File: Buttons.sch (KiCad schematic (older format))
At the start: 24 parts

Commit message: Probably pre-alpha version is done
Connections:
- net Button_+ renamed Button_Plus
- net Button_- renamed Button_Minus
- net Button_clock renamed Button_Clock
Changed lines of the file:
@@
 $Descr A4 11693 8268
 encoding utf-8
-Sheet 10 9
+Sheet 9 9
 Title ""
 Date ""
@@
 "Func"
 Text HLabel 3670 2030 0    50   Output ~ 0
-Button_+
+Button_Plus
 Text HLabel 3670 2470 0    50   Output ~ 0
-Button_-
+Button_Minus
 Text HLabel 3670 2910 0    50   Output ~ 0
 Button_Emh
 Text HLabel 3670 3350 0    50   Output ~ 0
-Button_clock
+Button_Clock
 Text HLabel 3670 3790 0    50   Output ~ 0
 Button_pH

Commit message: v0.1
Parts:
- gave numbers to parts that had none: 24

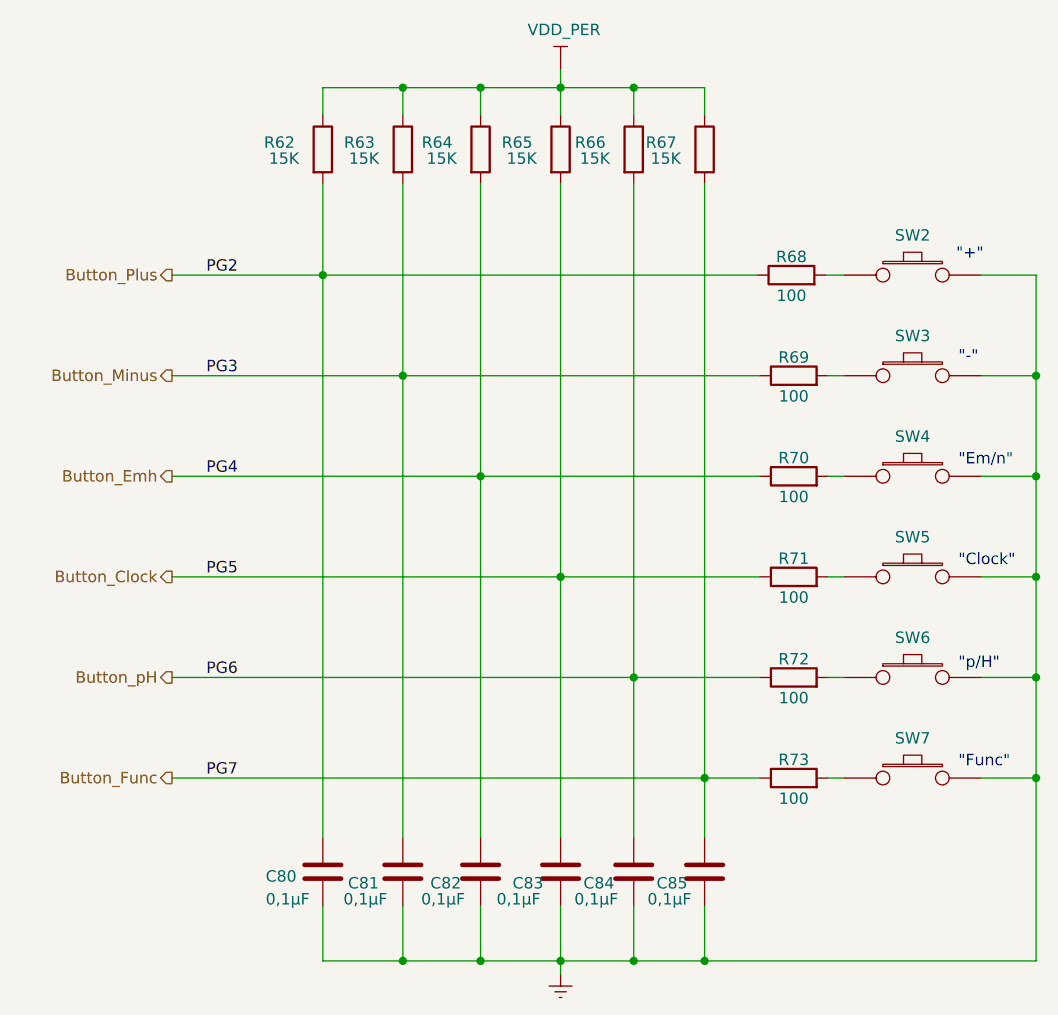
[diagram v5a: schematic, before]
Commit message: v0.3 changed sd_card holder
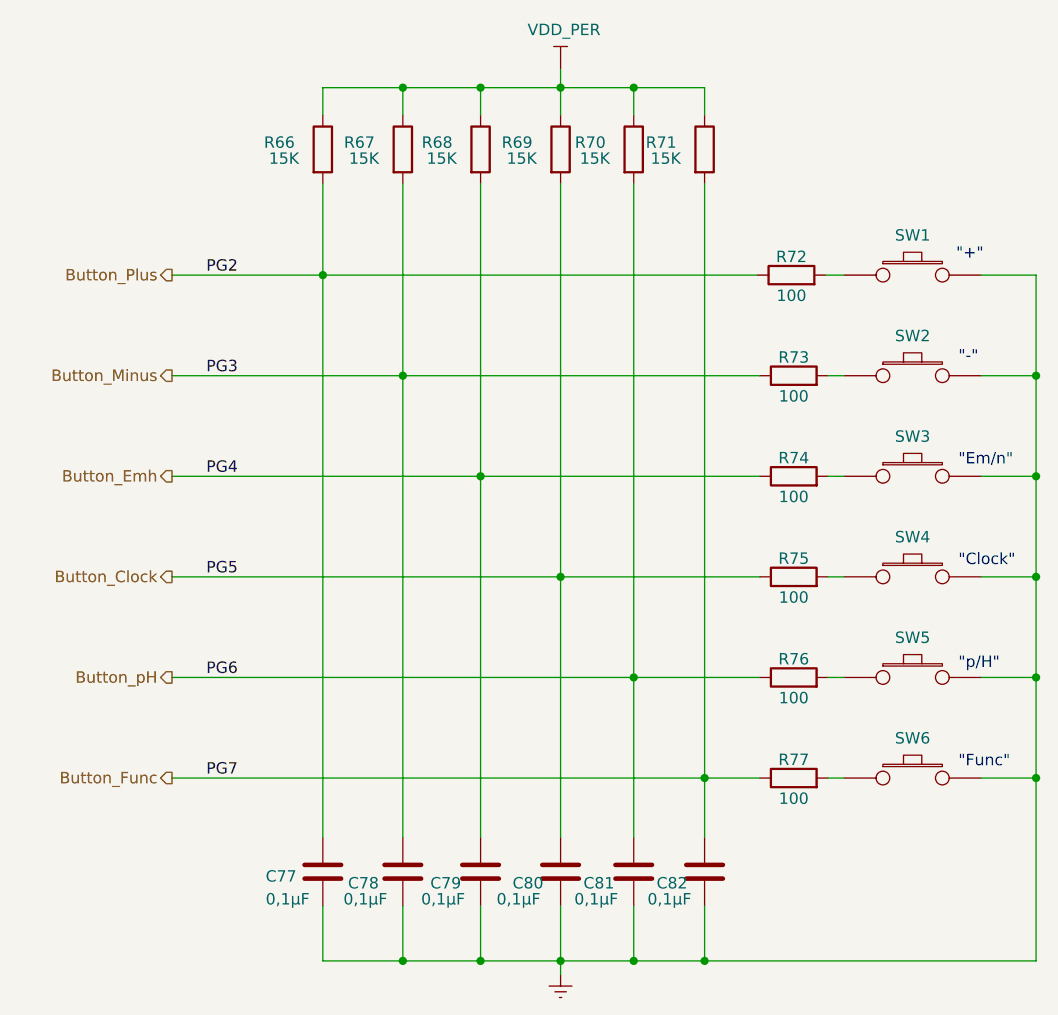
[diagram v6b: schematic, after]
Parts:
- renumbered C80 to C77, C81 to C78, C82 to C79, C83 to C80, C84 to C81, C85 to C82, R62 to R66, R63 to R67, R64 to R68, R65 to R69, R66 to R70, R67 to R71, R68 to R72, R69 to R73, R70 to R74, R71 to R75, R72 to R76, R73 to R77, SW2 to SW1, SW3 to SW2, SW4 to SW3, SW5 to SW4, SW6 to SW5, SW7 to SW6

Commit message: footprints associations is done
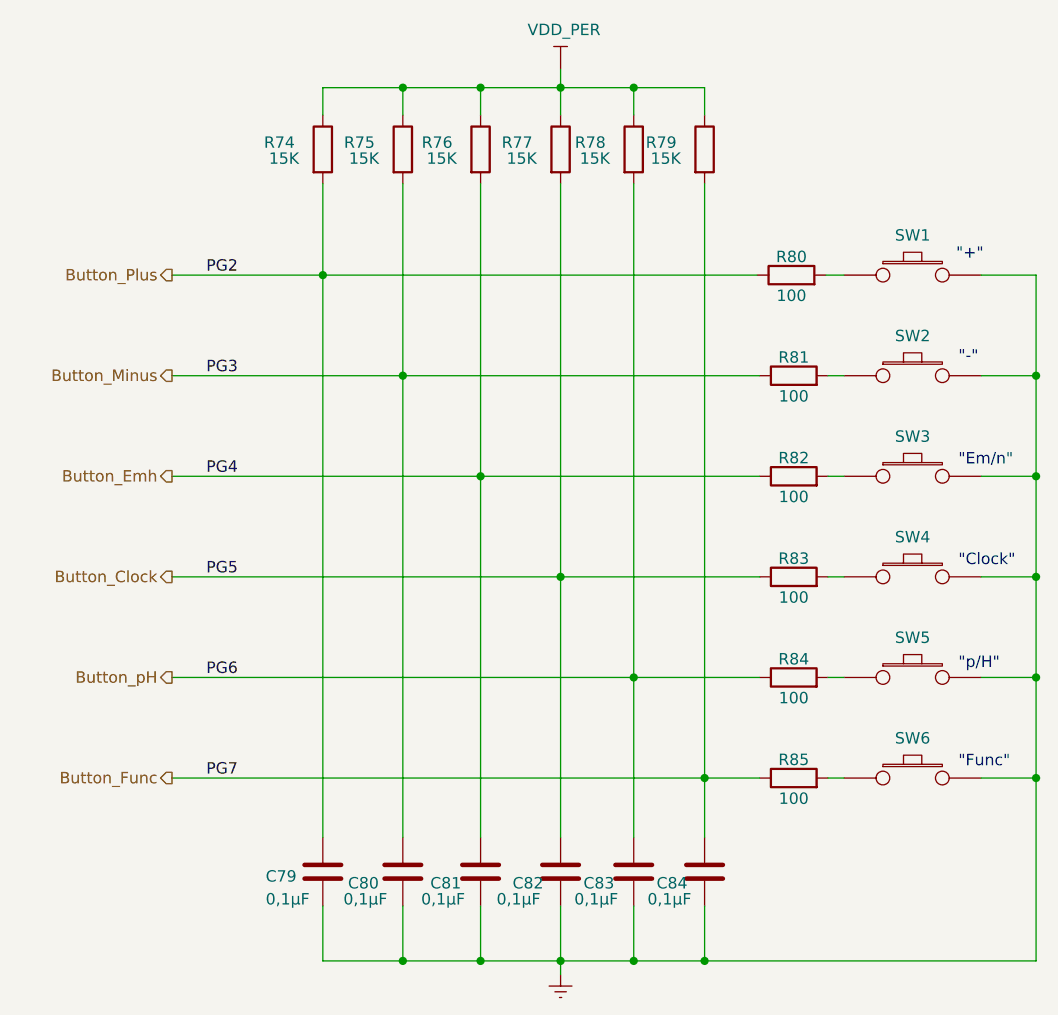
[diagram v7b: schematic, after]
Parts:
- C79: renamed from C77; Type CL10B105KA8NNNC -> C0603C104K5RACTU
- C81: renamed from C79; Type CL10B105KA8NNNC -> C0603C104K5RACTU
- C82: renamed from C80; Type CL10B105KA8NNNC -> C0603C104K5RACTU
- C83: renamed from C81; Type CL10B105KA8NNNC -> C0603C104K5RACTU
- C84: renamed from C82; Type CL10B105KA8NNNC -> C0603C104K5RACTU
- renumbered C78 to C80, R66 to R74, R67 to R75, R68 to R76, R69 to R77, R70 to R78, R71 to R79, R72 to R80, R73 to R81, R74 to R82, R75 to R83, R76 to R84, R77 to R85
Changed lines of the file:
@@
 Title "ШВУ"
 Date "2021-03-25"
-Rev "V0.1"
+Rev "V0.3"
 Comp "ЦВЕТМЕТНАЛАДКА"
 Comment1 "Шустов В.И."
@@
 AR Path="/60A03F8A/60D37702" Ref="R?"  Part="1"
 AR Path="/60D8C564/60D37702" Ref="R?"  Part="1"
-AR Path="/60CDBD15/60D37702" Ref="R71"  Part="1"
-F 0 "R71" H 5810 1510 50  0000 C CNN
+AR Path="/60CDBD15/60D37702" Ref="R79"  Part="1"
+F 0 "R79" H 5810 1510 50  0000 C CNN
 F 1 "15K" H 5830 1440 50  0000 C CNN
 F 2 "Resistor_SMD:R_0805_2012Metric_Pad1.20x1.40mm_HandSolder" V 5930 1480 50  0001 C CNN
@@
 AR Path="/60A03F8A/60D37D0B" Ref="R?"  Part="1"
 AR Path="/60D8C564/60D37D0B" Ref="R?"  Part="1"
-AR Path="/60CDBD15/60D37D0B" Ref="R70"  Part="1"
-F 0 "R70" H 5500 1510 50  0000 C CNN
+AR Path="/60CDBD15/60D37D0B" Ref="R78"  Part="1"
+F 0 "R78" H 5500 1510 50  0000 C CNN
 F 1 "15K" H 5520 1440 50  0000 C CNN
 F 2 "Resistor_SMD:R_0805_2012Metric_Pad1.20x1.40mm_HandSolder" V 5620 1480 50  0001 C CNN
@@
 AR Path="/60A03F8A/60D380ED" Ref="R?"  Part="1"
 AR Path="/60D8C564/60D380ED" Ref="R?"  Part="1"
-AR Path="/60CDBD15/60D380ED" Ref="R69"  Part="1"
-F 0 "R69" H 5180 1510 50  0000 C CNN
+AR Path="/60CDBD15/60D380ED" Ref="R77"  Part="1"
+F 0 "R77" H 5180 1510 50  0000 C CNN
 F 1 "15K" H 5200 1440 50  0000 C CNN
 F 2 "Resistor_SMD:R_0805_2012Metric_Pad1.20x1.40mm_HandSolder" V 5300 1480 50  0001 C CNN
@@
 AR Path="/60A03F8A/60D38BD5" Ref="R?"  Part="1"
 AR Path="/60D8C564/60D38BD5" Ref="R?"  Part="1"
-AR Path="/60CDBD15/60D38BD5" Ref="R68"  Part="1"
-F 0 "R68" H 4830 1510 50  0000 C CNN
+AR Path="/60CDBD15/60D38BD5" Ref="R76"  Part="1"
+F 0 "R76" H 4830 1510 50  0000 C CNN
 F 1 "15K" H 4850 1440 50  0000 C CNN
 F 2 "Resistor_SMD:R_0805_2012Metric_Pad1.20x1.40mm_HandSolder" V 4950 1480 50  0001 C CNN
@@
 AR Path="/60A03F8A/60D38EF4" Ref="R?"  Part="1"
 AR Path="/60D8C564/60D38EF4" Ref="R?"  Part="1"
-AR Path="/60CDBD15/60D38EF4" Ref="R67"  Part="1"
-F 0 "R67" H 4490 1510 50  0000 C CNN
+AR Path="/60CDBD15/60D38EF4" Ref="R75"  Part="1"
+F 0 "R75" H 4490 1510 50  0000 C CNN
 F 1 "15K" H 4510 1440 50  0000 C CNN
 F 2 "Resistor_SMD:R_0805_2012Metric_Pad1.20x1.40mm_HandSolder" V 4610 1480 50  0001 C CNN
@@
 AR Path="/60A03F8A/60D39378" Ref="R?"  Part="1"
 AR Path="/60D8C564/60D39378" Ref="R?"  Part="1"
-AR Path="/60CDBD15/60D39378" Ref="R66"  Part="1"
-F 0 "R66" H 4140 1510 50  0000 C CNN
+AR Path="/60CDBD15/60D39378" Ref="R74"  Part="1"
+F 0 "R74" H 4140 1510 50  0000 C CNN
 F 1 "15K" H 4160 1440 50  0000 C CNN
 F 2 "Resistor_SMD:R_0805_2012Metric_Pad1.20x1.40mm_HandSolder" V 4260 1480 50  0001 C CNN
@@
 AR Path="/60A03F8A/60D4289D" Ref="R?"  Part="1"
 AR Path="/60D8C564/60D4289D" Ref="R?"  Part="1"
-AR Path="/60CDBD15/60D4289D" Ref="R72"  Part="1"
-F 0 "R72" V 6460 2030 50  0000 C CNN
+AR Path="/60CDBD15/60D4289D" Ref="R80"  Part="1"
+F 0 "R80" V 6460 2030 50  0000 C CNN
 F 1 "100" V 6290 2030 50  0000 C CNN
 F 2 "Resistor_SMD:R_0805_2012Metric_Pad1.20x1.40mm_HandSolder" V 6310 2030 50  0001 C CNN
@@
 AR Path="/60A03F8A/60D436EA" Ref="C?"  Part="1"
 AR Path="/60D8C564/60D436EA" Ref="C?"  Part="1"
-AR Path="/60CDBD15/60D436EA" Ref="C77"  Part="1"
-F 0 "C77" H 4080 4620 50  0000 L CNN
+AR Path="/60CDBD15/60D436EA" Ref="C79"  Part="1"
+F 0 "C79" H 4080 4620 50  0000 L CNN
 F 1 "0,1µF" H 4080 4520 50  0000 L CNN
 F 2 "Capacitor_SMD:C_0603_1608Metric_Pad1.08x0.95mm_HandSolder" H 4368 4490 50  0001 C CNN
 F 3 "http://www.farnell.com/datasheets/2710676.pdf" H 4330 4640 50  0001 C CNN
-F 4 "CL10B105KA8NNNC" H 4330 4640 50  0001 C CNN "Type"
+F 4 "C0603C104K5RACTU" H 4330 4640 50  0001 C CNN "Type"
 	1    4330 4640
 	1    0    0    -1
@@
 AR Path="/60A03F8A/60D44563" Ref="C?"  Part="1"
 AR Path="/60D8C564/60D44563" Ref="C?"  Part="1"
-AR Path="/60CDBD15/60D44563" Ref="C78"  Part="1"
-F 0 "C78" H 4440 4590 50  0000 L CNN
+AR Path="/60CDBD15/60D44563" Ref="C80"  Part="1"
+F 0 "C80" H 4440 4590 50  0000 L CNN
 F 1 "0,1µF" H 4420 4520 50  0000 L CNN
 F 2 "Capacitor_SMD:C_0603_1608Metric_Pad1.08x0.95mm_HandSolder" H 4718 4490 50  0001 C CNN
@@
 AR Path="/60A03F8A/60D44905" Ref="C?"  Part="1"
 AR Path="/60D8C564/60D44905" Ref="C?"  Part="1"
-AR Path="/60CDBD15/60D44905" Ref="C79"  Part="1"
-F 0 "C79" H 4800 4590 50  0000 L CNN
+AR Path="/60CDBD15/60D44905" Ref="C81"  Part="1"
+F 0 "C81" H 4800 4590 50  0000 L CNN
 F 1 "0,1µF" H 4760 4520 50  0000 L CNN
 F 2 "Capacitor_SMD:C_0603_1608Metric_Pad1.08x0.95mm_HandSolder" H 5058 4490 50  0001 C CNN
 F 3 "http://www.farnell.com/datasheets/2710676.pdf" H 5020 4640 50  0001 C CNN
-F 4 "CL10B105KA8NNNC" H 5020 4640 50  0001 C CNN "Type"
+F 4 "C0603C104K5RACTU" H 5020 4640 50  0001 C CNN "Type"
 	1    5020 4640
 	1    0    0    -1
@@
 AR Path="/60A03F8A/60D44D94" Ref="C?"  Part="1"
 AR Path="/60D8C564/60D44D94" Ref="C?"  Part="1"
-AR Path="/60CDBD15/60D44D94" Ref="C80"  Part="1"
-F 0 "C80" H 5160 4590 50  0000 L CNN
+AR Path="/60CDBD15/60D44D94" Ref="C82"  Part="1"
+F 0 "C82" H 5160 4590 50  0000 L CNN
 F 1 "0,1µF" H 5090 4520 50  0000 L CNN
 F 2 "Capacitor_SMD:C_0603_1608Metric_Pad1.08x0.95mm_HandSolder" H 5408 4490 50  0001 C CNN
 F 3 "http://www.farnell.com/datasheets/2710676.pdf" H 5370 4640 50  0001 C CNN
-F 4 "CL10B105KA8NNNC" H 5370 4640 50  0001 C CNN "Type"
+F 4 "C0603C104K5RACTU" H 5370 4640 50  0001 C CNN "Type"
 	1    5370 4640
 	1    0    0    -1
@@
 AR Path="/60A03F8A/60D452B1" Ref="C?"  Part="1"
 AR Path="/60D8C564/60D452B1" Ref="C?"  Part="1"
-AR Path="/60CDBD15/60D452B1" Ref="C81"  Part="1"
-F 0 "C81" H 5470 4590 50  0000 L CNN
+AR Path="/60CDBD15/60D452B1" Ref="C83"  Part="1"
+F 0 "C83" H 5470 4590 50  0000 L CNN
 F 1 "0,1µF" H 5430 4520 50  0000 L CNN
 F 2 "Capacitor_SMD:C_0603_1608Metric_Pad1.08x0.95mm_HandSolder" H 5728 4490 50  0001 C CNN
 F 3 "http://www.farnell.com/datasheets/2710676.pdf" H 5690 4640 50  0001 C CNN
-F 4 "CL10B105KA8NNNC" H 5690 4640 50  0001 C CNN "Type"
+F 4 "C0603C104K5RACTU" H 5690 4640 50  0001 C CNN "Type"
 	1    5690 4640
 	1    0    0    -1
@@
 AR Path="/60A03F8A/60D456CF" Ref="C?"  Part="1"
 AR Path="/60D8C564/60D456CF" Ref="C?"  Part="1"
-AR Path="/60CDBD15/60D456CF" Ref="C82"  Part="1"
-F 0 "C82" H 5790 4590 50  0000 L CNN
+AR Path="/60CDBD15/60D456CF" Ref="C84"  Part="1"
+F 0 "C84" H 5790 4590 50  0000 L CNN
 F 1 "0,1µF" H 5750 4520 50  0000 L CNN
 F 2 "Capacitor_SMD:C_0603_1608Metric_Pad1.08x0.95mm_HandSolder" H 6038 4490 50  0001 C CNN
 F 3 "http://www.farnell.com/datasheets/2710676.pdf" H 6000 4640 50  0001 C CNN
-F 4 "CL10B105KA8NNNC" H 6000 4640 50  0001 C CNN "Type"
+F 4 "C0603C104K5RACTU" H 6000 4640 50  0001 C CNN "Type"
 	1    6000 4640
 	1    0    0    -1
@@
 AR Path="/60A03F8A/60D705B6" Ref="R?"  Part="1"
 AR Path="/60D8C564/60D705B6" Ref="R?"  Part="1"
-AR Path="/60CDBD15/60D705B6" Ref="R73"  Part="1"
-F 0 "R73" V 6470 2470 50  0000 C CNN
+AR Path="/60CDBD15/60D705B6" Ref="R81"  Part="1"
+F 0 "R81" V 6470 2470 50  0000 C CNN
 F 1 "100" V 6300 2470 50  0000 C CNN
 F 2 "Resistor_SMD:R_0805_2012Metric_Pad1.20x1.40mm_HandSolder" V 6320 2470 50  0001 C CNN
@@
 AR Path="/60A03F8A/60D70A21" Ref="R?"  Part="1"
 AR Path="/60D8C564/60D70A21" Ref="R?"  Part="1"
-AR Path="/60CDBD15/60D70A21" Ref="R74"  Part="1"
-F 0 "R74" V 6470 2910 50  0000 C CNN
+AR Path="/60CDBD15/60D70A21" Ref="R82"  Part="1"
+F 0 "R82" V 6470 2910 50  0000 C CNN
 F 1 "100" V 6300 2910 50  0000 C CNN
 F 2 "Resistor_SMD:R_0805_2012Metric_Pad1.20x1.40mm_HandSolder" V 6320 2910 50  0001 C CNN
@@
 AR Path="/60A03F8A/60D70FF6" Ref="R?"  Part="1"
 AR Path="/60D8C564/60D70FF6" Ref="R?"  Part="1"
-AR Path="/60CDBD15/60D70FF6" Ref="R75"  Part="1"
-F 0 "R75" V 6470 3350 50  0000 C CNN
+AR Path="/60CDBD15/60D70FF6" Ref="R83"  Part="1"
+F 0 "R83" V 6470 3350 50  0000 C CNN
 F 1 "100" V 6300 3350 50  0000 C CNN
 F 2 "Resistor_SMD:R_0805_2012Metric_Pad1.20x1.40mm_HandSolder" V 6320 3350 50  0001 C CNN
@@
 AR Path="/60A03F8A/60D714A5" Ref="R?"  Part="1"
 AR Path="/60D8C564/60D714A5" Ref="R?"  Part="1"
-AR Path="/60CDBD15/60D714A5" Ref="R76"  Part="1"
-F 0 "R76" V 6470 3790 50  0000 C CNN
+AR Path="/60CDBD15/60D714A5" Ref="R84"  Part="1"
+F 0 "R84" V 6470 3790 50  0000 C CNN
 F 1 "100" V 6300 3790 50  0000 C CNN
 F 2 "Resistor_SMD:R_0805_2012Metric_Pad1.20x1.40mm_HandSolder" V 6320 3790 50  0001 C CNN
@@
 AR Path="/60A03F8A/60D719AD" Ref="R?"  Part="1"
 AR Path="/60D8C564/60D719AD" Ref="R?"  Part="1"
-AR Path="/60CDBD15/60D719AD" Ref="R77"  Part="1"
-F 0 "R77" V 6470 4230 50  0000 C CNN
+AR Path="/60CDBD15/60D719AD" Ref="R85"  Part="1"
+F 0 "R85" V 6470 4230 50  0000 C CNN
 F 1 "100" V 6300 4230 50  0000 C CNN
 F 2 "Resistor_SMD:R_0805_2012Metric_Pad1.20x1.40mm_HandSolder" V 6320 4230 50  0001 C CNN
@@
 AR Path="/60D8A576" Ref="#PWR?"  Part="1"
 AR Path="/60A03F8A/60D8A576" Ref="#PWR?"  Part="1"
-AR Path="/60CDBD15/60D8A576" Ref="#PWR0107"  Part="1"
-F 0 "#PWR0107" H 5370 4840 50  0001 C CNN
+AR Path="/60CDBD15/60D8A576" Ref="#PWR0110"  Part="1"
+F 0 "#PWR0110" H 5370 4840 50  0001 C CNN
 F 1 "GNDREF" V 5375 4962 50  0001 R CNN
 F 2 "" H 5370 5090 50  0001 C CNN
@@
 P 5370 1130
 AR Path="/60D8C564/60D8F79A" Ref="#PWR?"  Part="1"
-AR Path="/60CDBD15/60D8F79A" Ref="#PWR0106"  Part="1"
-F 0 "#PWR0106" H 5370 980 50  0001 C CNN
+AR Path="/60CDBD15/60D8F79A" Ref="#PWR0109"  Part="1"
+F 0 "#PWR0109" H 5370 980 50  0001 C CNN
 F 1 "VDD_PER" H 5385 1303 50  0000 C CNN
 F 2 "" H 5370 1130 50  0001 C CNN
